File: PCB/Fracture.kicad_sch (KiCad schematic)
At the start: 46 parts, among them CN1 PJ-320D_C521460, J1 Barrel_Jack, J2 Conn_01x02, P1 USB_C_Plug, SW1 SW_Push, SW2 SW_Push, SW3 SW_SPDT, U1 ESP32-S3-WROOM-1-N4, U2 LM2596SX-5.0/NOPB, U3 AMS1117-3.3, U4 AMS1117-3.3, U5 74HC4067PW,118, U6 74HC4067PW,118, U7 GH39FKSW, U8 SP3485EN-L/TR

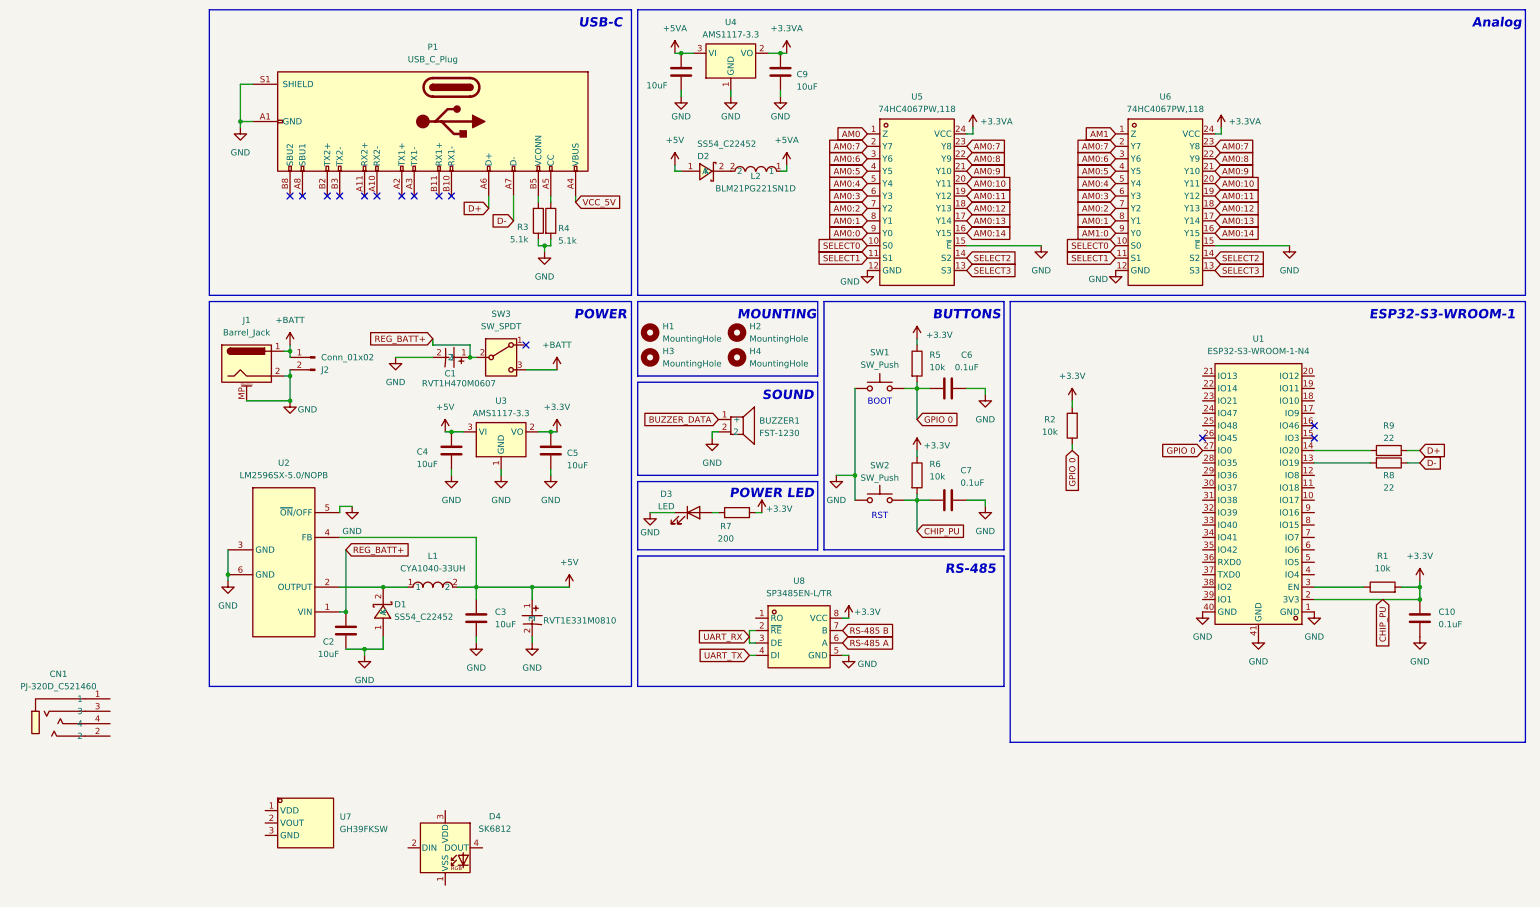
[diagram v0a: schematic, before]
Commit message: Schematic Done + PCB Layout Done
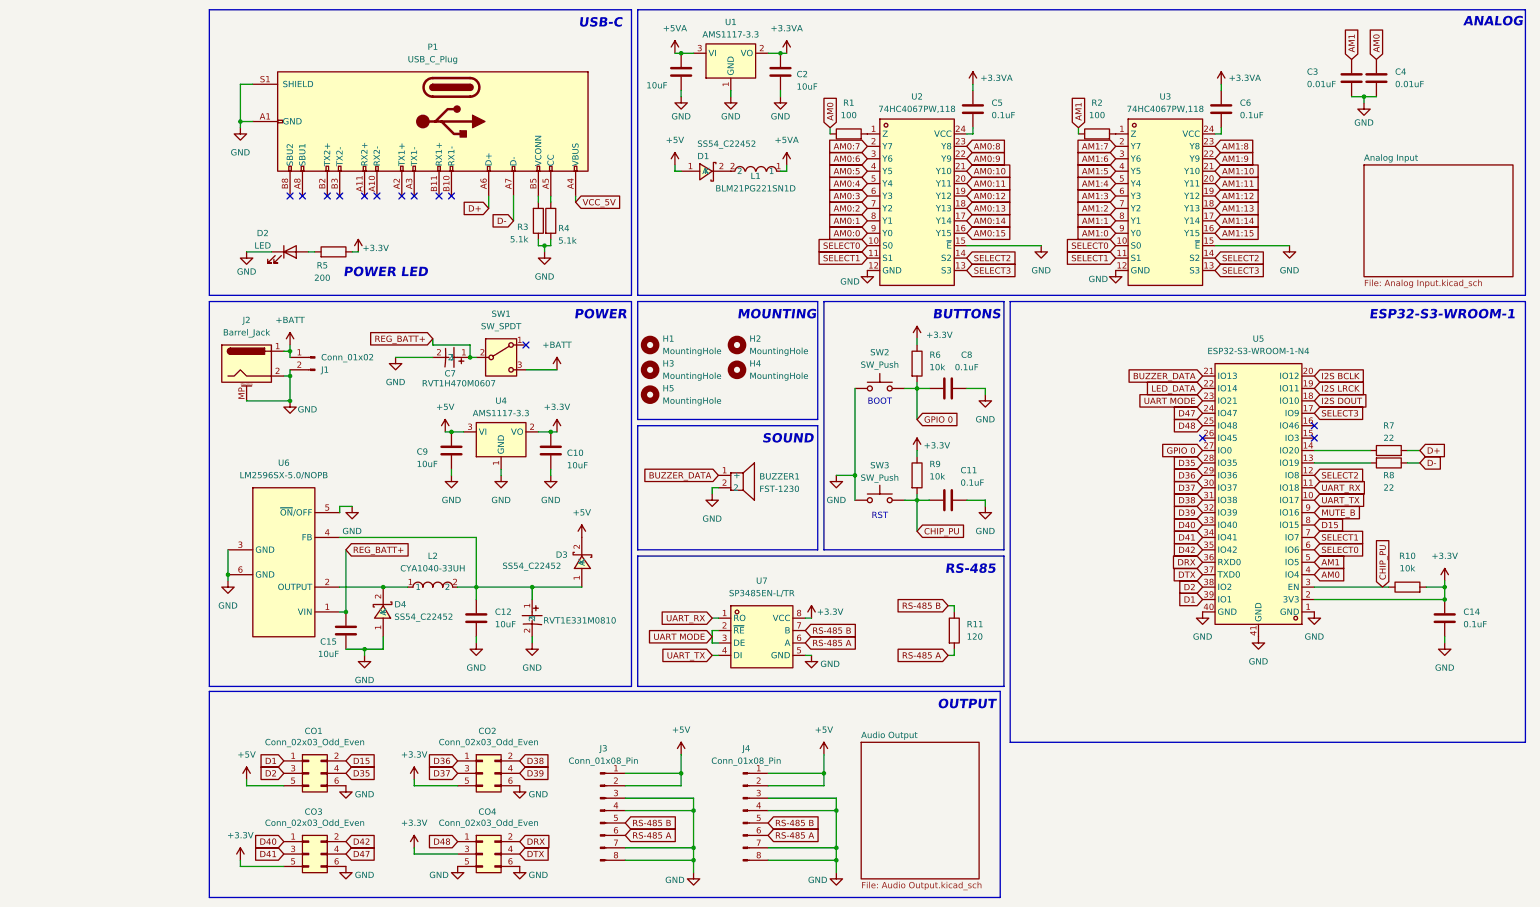
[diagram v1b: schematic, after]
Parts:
- removed CN1: PJ-320D_C521460, imported_components:AUDIO-SMD_PJ-320D, symbol imported_components:PJ-320D_C521460
- removed D4: SK6812, LED_SMD:LED_SK6812_PLCC4_5.0x5.0mm_P3.2mm, symbol LED:SK6812
- removed U7: GH39FKSW, imported_components:SOT-23-3_L2.9-W1.3-P1.90-LS2.4-BR, symbol imported_components:GH39FKSW
- added C3, C4: 0.01uF, imported_components:C0805, symbol Device:C
- added C5, C6: 0.1uF, imported_components:C0805, symbol Device:C
- added CO1, CO2, CO3, CO4: Conn_02x03_Odd_Even, imported_components:HDR-SMD_6P-P2.54-V, symbol Connector_Generic:Conn_02x03_Odd_Even
- added D3: SS54_C22452, imported_components:SMA_L4.4-W2.8-LS5.4-R-RD, symbol imported_components:SS54_C22452
- added H5: MountingHole, MountingHole:MountingHole_3.2mm_M3_Pad_Via, symbol Mechanical:MountingHole
- added J3, J4: Conn_01x08_Pin, Connector_PinHeader_2.54mm:PinHeader_1x08_P2.54mm_Vertical, symbol Connector:Conn_01x08_Pin
- added R1: 100, imported_components:R0805, symbol Device:R
- added R11: 120, imported_components:R0805, symbol Device:R
- C14: renamed from C10; footprint (none) -> imported_components:C0805
- J1: renamed from J2; footprint imported_components:CONN-TH_P5.00_KF301-5.0-2P -> Connector_PinHeader_2.54mm:PinHeader_1x02_P2.54mm_Vertical
- R10: renamed from R1; footprint (none) -> imported_components:R0805
- R2: value 10k -> 100; footprint (none) -> imported_components:R0805
- R7: renamed from R9; footprint (none) -> imported_components:R0805
- R8: footprint (none) -> imported_components:R0805
- renumbered C8 to C1, C5 to C10, C7 to C11, C3 to C12, C19 to C13, C2 to C15, C9 to C2, C1 to C7, C6 to C8, C4 to C9, D2 to D1, D3 to D2, D1 to D4, J1 to J2, L2 to L1, L1 to L2, R7 to R5, R5 to R6, R6 to R9, SW3 to SW1, SW1 to SW2, SW2 to SW3, U4 to U1, U5 to U2, U6 to U3, U3 to U4, U1 to U5, U2 to U6, U8 to U7
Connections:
- net +3.3V: now also CO2.5 (Pin_5), CO3.5 (Pin_5), CO4.3 (Pin_3); no longer C11.1, R2.2, R9.2, SW3.1
- net +3.3VA: now also C5.1, C6.1; no longer U2.24 (VCC), U3.24 (VCC)
- net +5V: now also CO1.5 (Pin_5), D3.2 (K), J3.1 (Pin_1), J3.2 (Pin_2), J4.1 (Pin_1), J4.2 (Pin_2); no longer C12.1, C13.1, L2.2, U6.4 (FB)
- net AM0: now also U5.4 (IO4), C4.1, R1.1; no longer U2.1 (Z)
- net AM0:1: no longer U3.8 (Y1)
- net AM0:10: now also U2.21 (Y10); no longer U2.20 (Y11), U3.20 (Y11)
- net AM0:11: now also U2.20 (Y11); no longer U2.19 (Y12), U3.19 (Y12)
- net AM0:12: now also U2.19 (Y12); no longer U2.18 (Y13), U3.18 (Y13)
- net AM0:13: now also U2.18 (Y13); no longer U2.17 (Y14), U3.17 (Y14)
- net AM0:14: now also U2.17 (Y14); no longer U2.16 (Y15), U3.16 (Y15)
- net AM0:2: no longer U3.7 (Y2)
- net AM0:3: no longer U3.6 (Y3)
- net AM0:4: no longer U3.5 (Y4)
- net AM0:5: no longer U3.4 (Y5)
- net AM0:6: no longer U3.3 (Y6)
- net AM0:7: no longer U2.23 (Y8), U3.2 (Y7), U3.23 (Y8)
- net AM0:8: now also U2.23 (Y8); no longer U2.22 (Y9), U3.22 (Y9)
- net AM0:9: now also U2.22 (Y9); no longer U2.21 (Y10), U3.21 (Y10)
- net AM1: now also R2.1, U5.5 (IO5), C3.1; no longer U3.1 (Z)
- net BUZZER_DATA: now also U5.21 (IO13)
- net GND: now also C3.2, C4.2, CO1.6 (Pin_6), CO2.6 (Pin_6), CO3.6 (Pin_6), CO4.5 (Pin_5), CO4.6 (Pin_6), J3.3 (Pin_3), J3.4 (Pin_4), J3.7 (Pin_7), J3.8 (Pin_8), J4.3 (Pin_3), J4.4 (Pin_4), J4.7 (Pin_7), J4.8 (Pin_8)
- net GPIO 0: no longer R2.1
- net RS-485 A: now also J3.6 (Pin_6), J4.6 (Pin_6), R11.2
- net RS-485 B: now also J3.5 (Pin_5), J4.5 (Pin_5), R11.1
- net SELECT0: now also U5.6 (IO6)
- net SELECT1: now also U5.7 (IO7)
- net SELECT2: now also U5.12 (IO8)
- net SELECT3: now also U5.17 (IO9)
- net UART_RX: now also U5.11 (IO18), U7.1 (RO); no longer U7.2 (~{RE}), U7.3 (DE)
- net UART_TX: now also U5.10 (IO17)
- net CHIP_PU: now reaches R10.1, U5.3 (EN)
- net CHIP_PU: now also C11.1, R9.2, SW3.1
- net I2S DOUT: now reaches U5.18 (IO10)
- net I2S LRCK: now reaches U5.19 (IO11)
- net I2S BCLK: now reaches U5.20 (IO12)
- net LED_DATA: now reaches U5.22 (IO14)
- net UART MODE: now reaches U5.23 (IO21)
- net UART MODE: now also U7.2 (~{RE}), U7.3 (DE)
- net D47: now reaches U5.24 (IO47)
- net D47: now also CO3.4 (Pin_4)
- net D48: now reaches U5.25 (IO48)
- net D48: now also CO4.1 (Pin_1)
- net D35: now reaches U5.28 (IO35)
- net D35: now also CO1.4 (Pin_4)
- net D36: now reaches U5.29 (IO36)
- net D36: now also CO2.1 (Pin_1)
- net D37: now reaches U5.30 (IO37)
- net D37: now also CO2.3 (Pin_3)
- net D38: now reaches U5.31 (IO38)
- net D38: now also CO2.2 (Pin_2)
- net D39: now reaches U5.32 (IO39)
- net D39: now also CO2.4 (Pin_4)
- net D40: now reaches U5.33 (IO40)
- net D40: now also CO3.1 (Pin_1)
- net D41: now reaches U5.34 (IO41)
- net D41: now also CO3.3 (Pin_3)
- net D42: now reaches U5.35 (IO42)
- net D42: now also CO3.2 (Pin_2)
- net DRX: now reaches U5.36 (RXD0)
- net DRX: now also CO4.2 (Pin_2)
- net DTX: now reaches U5.37 (TXD0)
- net DTX: now also CO4.4 (Pin_4)
- net D2: now reaches U5.38 (IO2)
- net D2: now also CO1.3 (Pin_3)
- net D1: now reaches U5.39 (IO1)
- net D1: now also CO1.1 (Pin_1)
- net D15: now reaches U5.8 (IO15)
- net D15: now also CO1.2 (Pin_2)
- net MUTE_B: now reaches U5.9 (IO16)
- new net: R1.2, U2.1 (Z)
- new net: C5.2, U2.24 (VCC)
- new net: C12.1, C13.1, D3.1 (A), L2.2, U6.4 (FB)
- new net: R2.2, U3.1 (Z)
- new net: C6.2, U3.24 (VCC)
- new net AM0:15: U2.16 (Y15)
- new net AM1:1: U3.8 (Y1)
- new net AM1:10: U3.21 (Y10)
- new net AM1:11: U3.20 (Y11)
- new net AM1:12: U3.19 (Y12)
- new net AM1:13: U3.18 (Y13)
- new net AM1:14: U3.17 (Y14)
- new net AM1:15: U3.16 (Y15)
- new net AM1:2: U3.7 (Y2)
- new net AM1:3: U3.6 (Y3)
- new net AM1:4: U3.5 (Y4)
- new net AM1:5: U3.4 (Y5)
- new net AM1:6: U3.3 (Y6)
- new net AM1:7: U3.2 (Y7)
- new net AM1:8: U3.23 (Y8)
- new net AM1:9: U3.22 (Y9)
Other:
- added sheet Analog Input (Analog Input.kicad_sch)
- added sheet Audio Output (Audio Output.kicad_sch)
- note added: "ANALOG"
- note added: "OUTPUT"
- note removed: "Analog"
- moved on the sheet: BUZZER1, C14, D2, H1, H2, H3, H4, R10, R5, U7

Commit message: PCB routing done
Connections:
- net VCC_5V is gone; now on net +5V: P1.A4 (VBUS), P1.A9 (VBUS), P1.B4 (VBUS), P1.B9 (VBUS)
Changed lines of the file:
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@@
 	(wire
 		(pts
+			(xy 88.9 53.34) (xy 93.98 53.34)
+		)
+		(stroke
+			(width 0)
+			(type default)
+		)
+	)
+	(wire
+		(pts
 			(xy 113.03 185.42) (xy 113.03 177.8)
 		)
@@
 		)
 	)
+	(global_label "D2"
+		(shape input)
+		(at 198.12 154.94 0)
+		(fields_autoplaced yes)
+		(effects
+			(font
+				(size 1.27 1.27)
+			)
+			(justify left)
+		)
+		(property "Intersheetrefs" "${INTERSHEET_REFS}"
+			(at 203.5847 154.94 0)
+			(effects
+				(font
+					(size 1.27 1.27)
+				)
+				(justify left)
+				(hide yes)
+			)
+		)
+	)
 	(global_label "AM1"
 		(shape input)
@@
 		)
 	)
+	(global_label "Encoder B"
+		(shape input)
+		(at 198.12 154.94 180)
+		(fields_autoplaced yes)
+		(effects
+			(font
+				(size 1.27 1.27)
+			)
+			(justify right)
+		)
+		(property "Intersheetrefs" "${INTERSHEET_REFS}"
+			(at 185.3378 154.94 0)
+			(effects
+				(font
+					(size 1.27 1.27)
+				)
+				(justify right)
+				(hide yes)
+			)
+		)
+	)
 	(global_label "RS-485 B"
 		(shape input)
@@
 		)
 	)
+	(global_label "Encoder A"
+		(shape input)
+		(at 198.12 152.4 180)
+		(fields_autoplaced yes)
+		(effects
+			(font
+				(size 1.27 1.27)
+			)
+			(justify right)
+		)
+		(property "Intersheetrefs" "${INTERSHEET_REFS}"
+			(at 185.5192 152.4 0)
+			(effects
+				(font
+					(size 1.27 1.27)
+				)
+				(justify right)
+				(hide yes)
+			)
+		)
+	)
 	(global_label "D38"
 		(shape input)
@@
 		)
 	)
-	(global_label "VCC_5V"
-		(shape input)
-		(at 88.9 53.34 0)
-		(fields_autoplaced yes)
-		(effects
-			(font
-				(size 1.27 1.27)
-			)
-			(justify left)
-		)
-		(property "Intersheetrefs" "${INTERSHEET_REFS}"
-			(at 98.7795 53.34 0)
-			(effects
-				(font
-					(size 1.27 1.27)
-				)
-				(justify left)
-				(hide yes)
-			)
-		)
-	)
 	(global_label "SELECT2"
 		(shape input)
@@
 		)
 	)
+	(global_label "Encoder SW 1"
+		(shape input)
+		(at 198.12 157.48 180)
+		(fields_autoplaced yes)
+		(effects
+			(font
+				(size 1.27 1.27)
+			)
+			(justify right)
+		)
+		(property "Intersheetrefs" "${INTERSHEET_REFS}"
+			(at 181.7698 157.48 0)
+			(effects
+				(font
+					(size 1.27 1.27)
+				)
+				(justify right)
+				(hide yes)
+			)
+		)
+	)
 	(global_label "AM0:15"
 		(shape input)
@@
 		)
 	)
+	(global_label "D15"
+		(shape input)
+		(at 198.12 157.48 0)
+		(fields_autoplaced yes)
+		(effects
+			(font
+				(size 1.27 1.27)
+			)
+			(justify left)
+		)
+		(property "Intersheetrefs" "${INTERSHEET_REFS}"
+			(at 204.7942 157.48 0)
+			(effects
+				(font
+					(size 1.27 1.27)
+				)
+				(justify left)
+				(hide yes)
+			)
+		)
+	)
 	(global_label "D1"
 		(shape input)
@@
 		)
 	)
+	(global_label "D1"
+		(shape input)
+		(at 198.12 152.4 0)
+		(fields_autoplaced yes)
+		(effects
+			(font
+				(size 1.27 1.27)
+			)
+			(justify left)
+		)
+		(property "Intersheetrefs" "${INTERSHEET_REFS}"
+			(at 203.5847 152.4 0)
+			(effects
+				(font
+					(size 1.27 1.27)
+				)
+				(justify left)
+				(hide yes)
+			)
+		)
+	)
 	(global_label "I2S LRCK"
 		(shape input)
@@
 					(unit 1)
 				)
+			)
+		)
+	)
+	(symbol
+		(lib_id "power:+5V")
+		(at 93.98 53.34 0)
+		(unit 1)
+		(exclude_from_sim no)
+		(in_bom yes)
+		(on_board yes)
+		(dnp no)
+		(fields_autoplaced yes)
+		(property "Reference" "#PWR0211"
+			(at 93.98 57.15 0)
+			(effects
+				(font
+					(size 1.27 1.27)
+				)
+				(hide yes)
+			)
+		)
+		(property "Value" "+5V"
+			(at 93.98 48.26 0)
+			(effects
+				(font
+					(size 1.27 1.27)
+				)
+			)
+		)
+		(property "Footprint" ""
+			(at 93.98 53.34 0)
+			(effects
+				(font
+					(size 1.27 1.27)
+				)
+				(hide yes)
+			)
+		)
+		(property "Datasheet" ""
+			(at 93.98 53.34 0)
+			(effects
+				(font
+					(size 1.27 1.27)
+				)
+				(hide yes)
+			)
+		)
+		(property "Description" "Power symbol creates a global label with name \"+5V\""
+			(at 93.98 53.34 0)
+			(effects
+				(font
+					(size 1.27 1.27)
+				)
+				(hide yes)
+			)
+		)
+		(pin "1"
+		)
+		(instances
+			(project "Fracture"
+				(path "/75221650-6511-45d6-90de-2d3fdbaa0af3"
+					(reference "#PWR0211")
+					(unit 1)
+				)
